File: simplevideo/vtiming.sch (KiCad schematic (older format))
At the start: 4 parts, among them U10 CD74HC40103, U11 CD74HC40103, U12 CD74HC40103, U13 74LS74

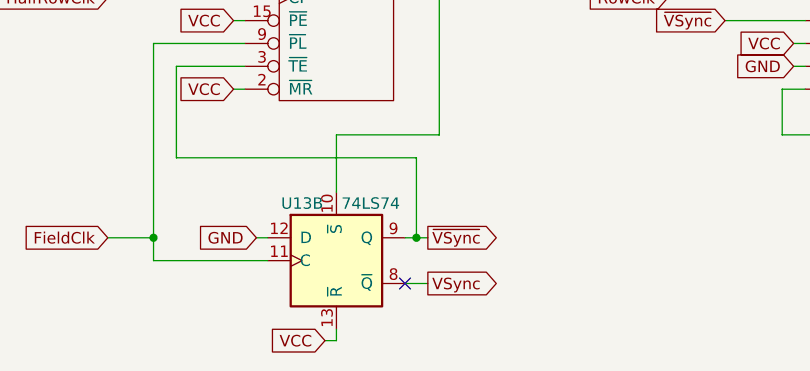
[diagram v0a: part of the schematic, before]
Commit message: Include 6502, ROM, etc in circuit, all laid out together
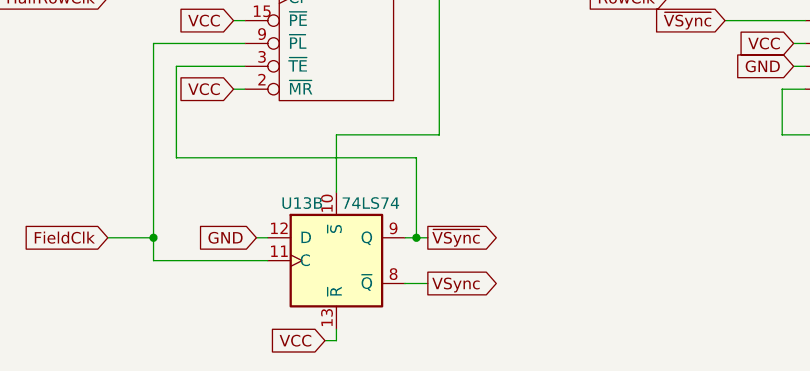
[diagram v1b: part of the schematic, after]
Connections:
- no-connect marks 1 -> 0
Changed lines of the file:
@@
 $Descr A4 11693 8268
 encoding utf-8
-Sheet 3 5
+Sheet 3 7
 Title ""
 Date ""
@@
 Text GLabel 6500 3400 2    50   Output ~ 0
 VOn
-NoConn ~ 2700 3400
 $EndSCHEMATC

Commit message: Fixed various issues discovered during building and testing
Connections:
- net GND: no longer U12.10 (P4), U12.12 (P6), U12.13 (P7), U12.4 (P0), U12.5 (P1), U12.7 (P3)
- net VCC: now also U12.12 (P6), U12.13 (P7), U12.7 (P3); no longer U11.6 (P2), U12.11 (P5), U12.6 (P2)
- new net ~NTSC: U11.6 (P2), U12.10 (P4), U12.11 (P5), U12.4 (P0), U12.5 (P1), U12.6 (P2)
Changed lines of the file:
@@
 VCC
 Text GLabel 4150 1750 0    50   Input ~ 0
-VCC
+~NTSC
 Text GLabel 4400 1650 0    50   Input ~ 0
 GND
@@
 Text GLabel 6650 2550 0    50   Input ~ 0
 VCC
-Text GLabel 6400 1450 0    50   Input ~ 0
-VCC
-Text GLabel 6400 1750 0    50   Input ~ 0
-VCC
-Text GLabel 6650 1650 0    50   Input ~ 0
-GND
-Text GLabel 6650 1550 0    50   Input ~ 0
-GND
-Text GLabel 6650 1950 0    50   Input ~ 0
-GND
-Text GLabel 6650 1350 0    50   Input ~ 0
-GND
-Text GLabel 6650 1250 0    50   Input ~ 0
-GND
-Text GLabel 6650 1850 0    50   Input ~ 0
-GND
+Text GLabel 6550 1450 0    50   Input ~ 0
+~NTSC
 Wire Wire Line
 	7550 1850 7550 2850
@@
 	6650 2550 6700 2550
 Wire Wire Line
-	6650 1850 6700 1850
+	6550 1850 6700 1850
 Wire Wire Line
-	6400 1750 6700 1750
+	6550 1750 6700 1750
 Wire Wire Line
-	6650 1650 6700 1650
+	6300 1650 6700 1650
 Wire Wire Line
-	6650 1550 6700 1550
+	6550 1550 6700 1550
 Wire Wire Line
-	6650 1350 6700 1350
+	6300 1350 6700 1350
 Wire Wire Line
-	6650 1250 6700 1250
+	6300 1250 6700 1250
 Wire Wire Line
-	6700 1950 6650 1950
+	6700 1950 6550 1950
 $Comp
 L g200kg_CD74HCxx:CD74HC40103 U?
@@
 $EndComp
 Wire Wire Line
-	6400 1450 6700 1450
+	6550 1450 6700 1450
 Text GLabel 4400 2450 0    50   Input ~ 0
 GND
@@
 Text GLabel 6500 3400 2    50   Output ~ 0
 VOn
+Text GLabel 6300 1250 0    50   Input ~ 0
+VCC
+Text GLabel 6300 1350 0    50   Input ~ 0
+VCC
+Text GLabel 6300 1650 0    50   Input ~ 0
+VCC
+Text GLabel 6550 1550 0    50   Input ~ 0
+~NTSC
+Text GLabel 6550 1750 0    50   Input ~ 0
+~NTSC
+Text GLabel 6550 1850 0    50   Input ~ 0
+~NTSC
+Text GLabel 6550 1950 0    50   Input ~ 0
+~NTSC
 $EndSCHEMATC
